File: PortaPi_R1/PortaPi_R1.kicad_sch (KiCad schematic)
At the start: 9 parts, among them J1 Raspberry_Pi_2_3, J2 USB_C_Receptacle, J3 AudioJack2_Ground, SW1 SW_Push, SW2 SW_Slide_DPDT, U1 BQ24072RGT, U2 TPS61252DSG, U3 LTC2942

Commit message: additions
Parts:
- added U4: BME680, Package_LGA:Bosch_LGA-8_3x3mm_P0.8mm_ClockwisePinNumbering, symbol Sensor:BME680
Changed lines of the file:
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@@
+	)
+	(symbol
+		(lib_id "Sensor:BME680")
+		(at 77.47 166.37 0)
+		(unit 1)
+		(exclude_from_sim no)
+		(in_bom yes)
+		(on_board yes)
+		(dnp no)
+		(fields_autoplaced yes)
+		(property "Reference" "U4"
+			(at 66.04 165.0999 0)
+			(effects
+				(font
+					(size 1.27 1.27)
+				)
+				(justify right)
+			)
+		)
+		(property "Value" "BME680"
+			(at 66.04 167.6399 0)
+			(effects
+				(font
+					(size 1.27 1.27)
+				)
+				(justify right)
+			)
+		)
+		(property "Footprint" "Package_LGA:Bosch_LGA-8_3x3mm_P0.8mm_ClockwisePinNumbering"
+			(at 114.3 177.8 0)
+			(effects
+				(font
+					(size 1.27 1.27)
+				)
+				(hide yes)
+			)
+		)
+		(property "Datasheet" "https://ae-bst.resource.bosch.com/media/_tech/media/datasheets/BST-BME680-DS001.pdf"
+			(at 77.47 171.45 0)
+			(effects
+				(font
+					(size 1.27 1.27)
+				)
+				(hide yes)
+			)
+		)
+		(property "Description" "4-in-1 sensor, gas, humidity, pressure, temperature, I2C and SPI interface, 1.71-3.6V, LGA-8"
+			(at 77.47 166.37 0)
+			(effects
+				(font
+					(size 1.27 1.27)
+				)
+				(hide yes)
+			)
+		)
+		(pin "4"
+		)
+		(pin "8"
+		)
+		(pin "5"
+		)
+		(pin "6"
+		)
+		(pin "2"
+		)
+		(pin "7"
+		)
+		(pin "1"
+		)
+		(pin "3"
+		)
+		(instances
+			(project ""
+				(path "/aef56874-4e02-4e4a-b6dd-7772aaa5a84e"
+					(reference "U4")
+					(unit 1)
+				)
+			)
+		)
 	)
 	(symbol

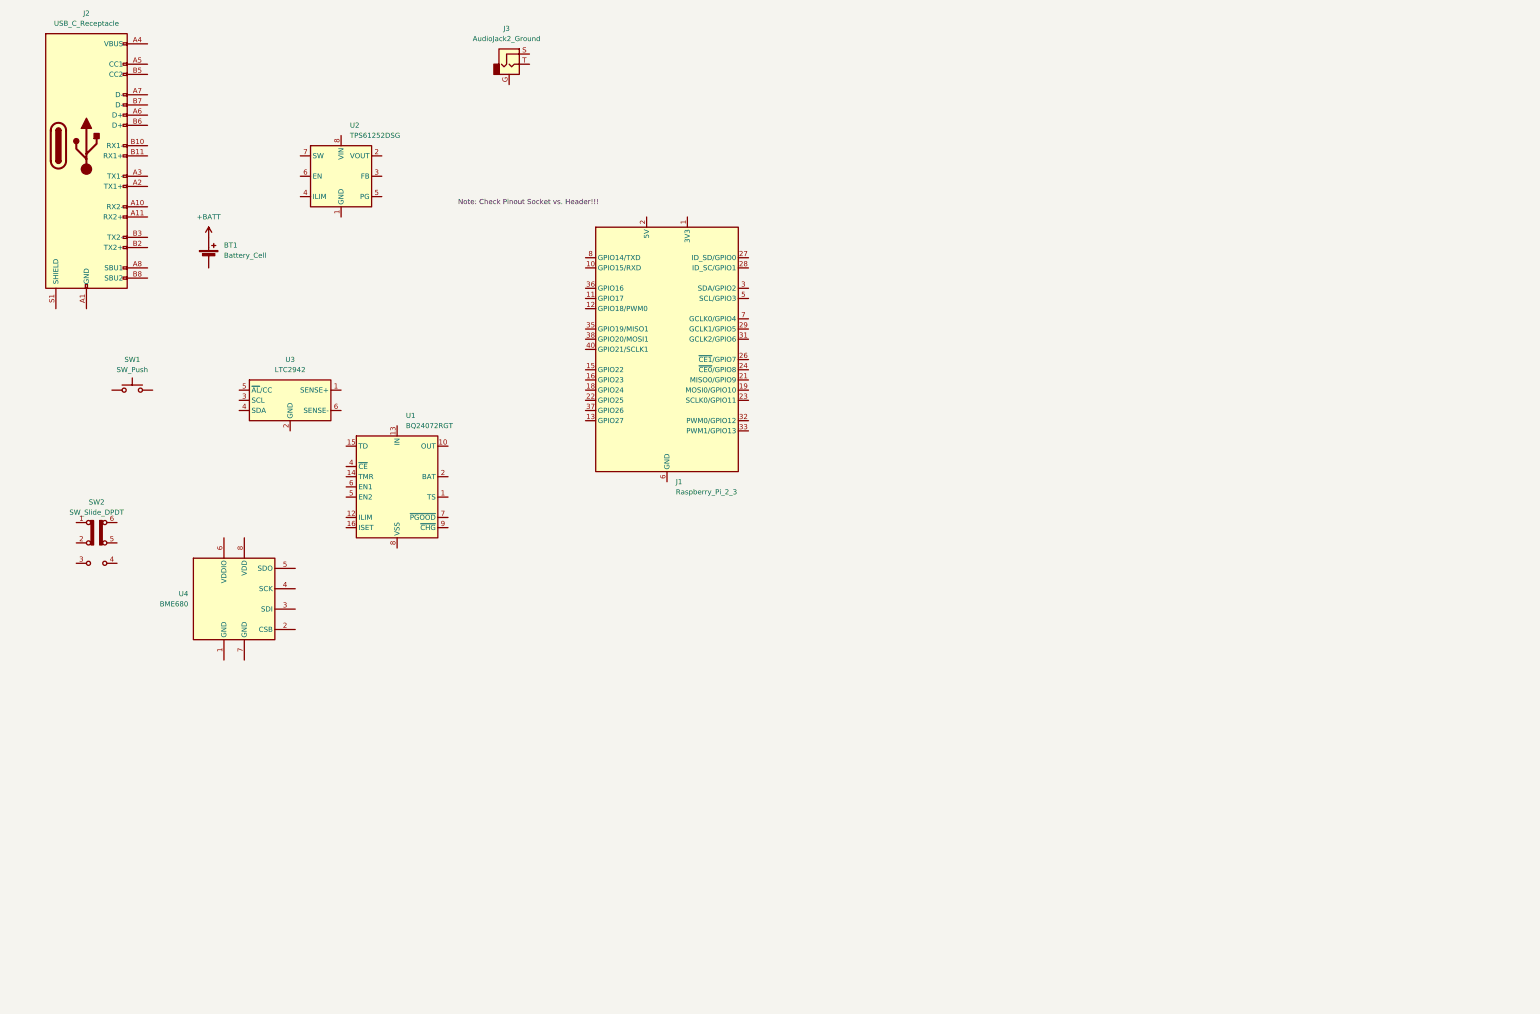
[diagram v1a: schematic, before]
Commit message: designed power path/regulator ect...
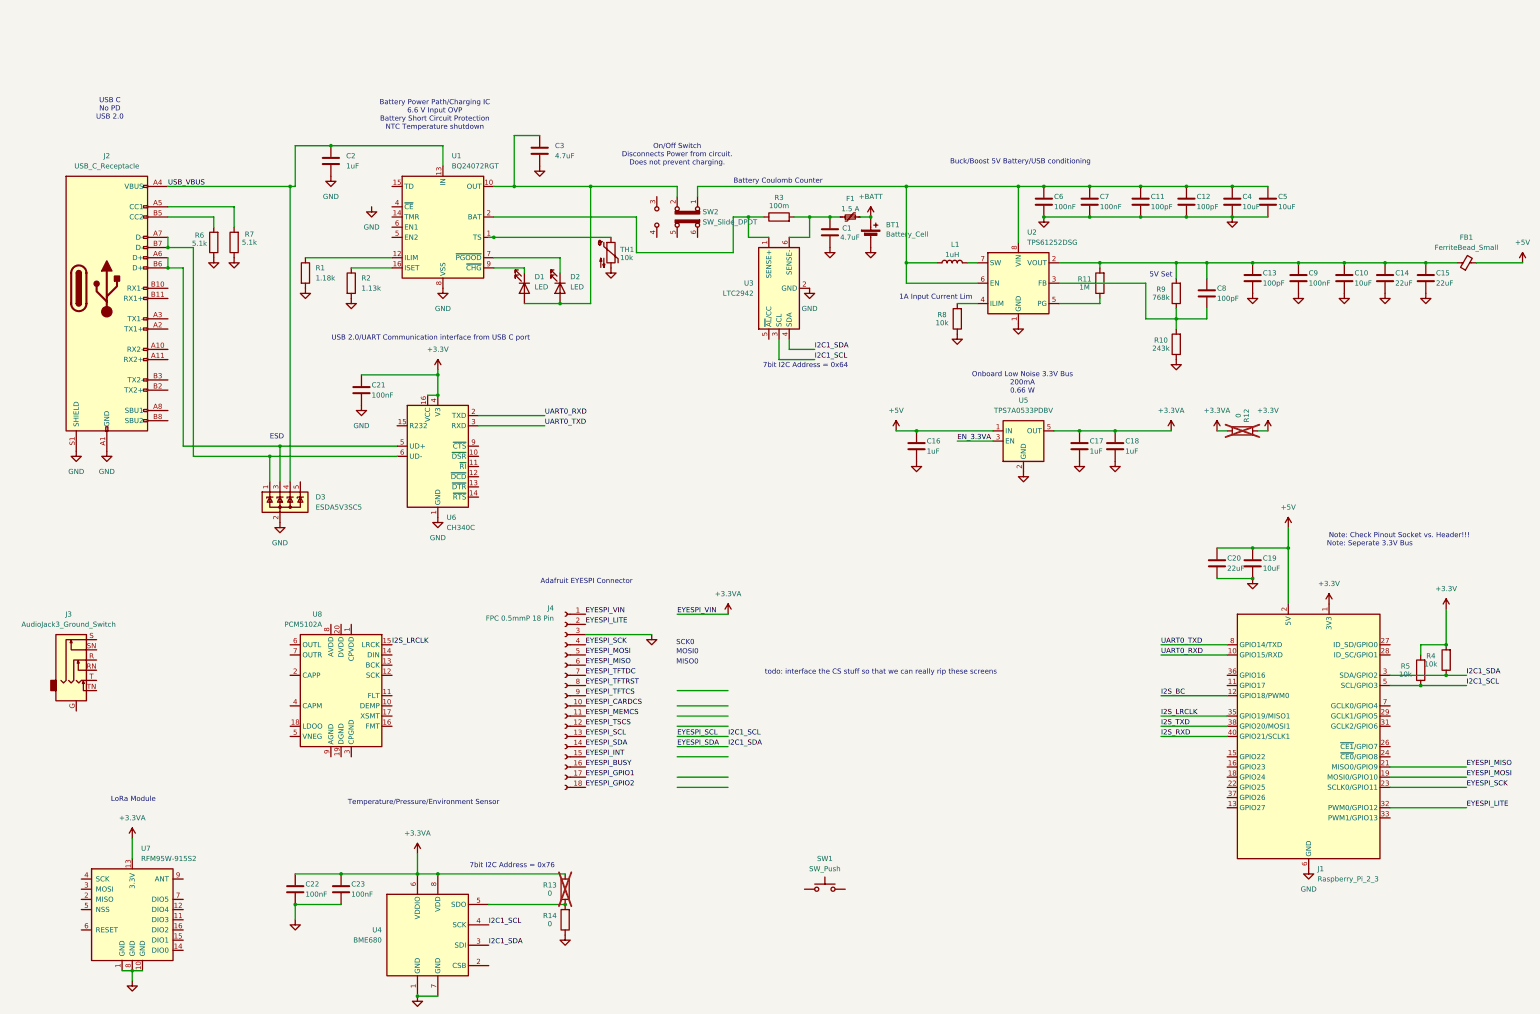
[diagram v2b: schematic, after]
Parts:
- removed J3: AudioJack2_Ground, symbol Connector_Audio:AudioJack2_Ground
- added C1, C3: 4.7uF, symbol Device:C
- added C10, C19, C4, C5: 10uF, symbol Device:C
- added C11, C12, C13, C8: 100pF, symbol Device:C
- added C14, C15, C20: 22uF, symbol Device:C
- added C16, C17, C18, C2: 1uF, symbol Device:C
- added C21, C22, C23, C6, C7, C9: 100nF, symbol Device:C
- added D1, D2: LED, symbol Device:LED
- added D3: ESDA5V3SC5, Package_TO_SOT_SMD:SOT-23-5, symbol Power_Protection:ESDA5V3SC5
- added F1: 1.5 A, symbol Device:Polyfuse_Small
- added FB1: FerriteBead_Small, symbol Device:FerriteBead_Small
- added J3: AudioJack3_Ground_Switch, symbol Connector_Audio:AudioJack3_Ground_Switch
- added J4: FPC 0.5mmP 18 Pin, Connector_FFC-FPC:TE_1-1734839-8_1x18-1MP_P0.5mm_Horizontal, symbol Connector:Conn_01x18_Socket
- added L1: 1uH, symbol Device:L
- added R1: 1.18k, symbol Device:R
- added R10: 243k, symbol Device:R
- added R11: 1M, symbol Device:R
- added R12, R13, R14: 0, symbol Device:R
- added R2: 1.13k, symbol Device:R
- added R3: 100m, symbol Device:R
- added R4, R5, R8: 10k, symbol Device:R
- added R6, R7: 5.1k, symbol Device:R
- added R9: 768k, symbol Device:R
- added TH1: 10k, symbol Device:Thermistor_NTC
- added U5: TPS7A0533PDBV, Package_TO_SOT_SMD:SOT-23-5, symbol Regulator_Linear:TPS7A0533PDBV
- added U6: CH340C, Package_SO:SOIC-16_3.9x9.9mm_P1.27mm, symbol Interface_USB:CH340C
- added U7: RFM95W-915S2, RF_Module:HOPERF_RFM9XW_SMD, symbol RF_Module:RFM95W-915S2
- added U8: PCM5102A, Package_SO:TSSOP-20_4.4x6.5mm_P0.65mm, symbol Audio:PCM5102A
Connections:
- net +BATT: now also F1.2
- net GND: now reaches U4.1 (GND)
- net GND: now also BT1.2 (-), J1.14 (GND), J1.20 (GND), J1.25 (GND), J1.30 (GND), J1.34 (GND), J1.39 (GND), J1.6 (GND), J1.9 (GND), J2.A1 (GND), J2.A12 (GND), J2.B1 (GND), J2.B12 (GND), J2.S1 (SHIELD), U1.17 (VSS), U1.8 (VSS), U2.1 (GND), U2.9 (GND), U3.2 (GND), U4.7 (GND), C1.2, C10.2, C11.2, C12.2, C13.2, C14.2, C15.2, C16.2, C17.2, C18.2, C19.2, C2.2, C20.2, C21.2, C22.2, C23.2, C3.2, C4.2, C5.2, C6.2, C7.2, C9.2, D3.2 (A), J4.3 (Pin_3), R1.2, R10.1, R14.1, R2.2, R6.1, R7.1, R8.1, TH1.2, U5.2 (GND), U6.1 (GND), U7.1 (GND), U7.10 (GND), U7.8 (GND)
- net EYESPI_SDA: now reaches U4.3 (SDI)
- net EYESPI_SDA: now also J1.3 (SDA/GPIO2), U3.4 (SDA), J4.14 (Pin_14), R4.1
- net EYESPI_SCL: now reaches U4.4 (SCK)
- net EYESPI_SCL: now also J1.5 (SCL/GPIO3), U3.3 (SCL), J4.13 (Pin_13), R5.1
- net at U4.5 (SDO): now also R13.1, R14.2
- net +3.3VA: now reaches U4.6 (VDDIO)
- net +3.3VA: now also U4.8 (VDD), C17.1, C18.1, C22.1, C23.1, J4.1 (Pin_1), R12.1, R13.2, U5.5 (OUT), U7.13 (3.3V)
- net at U2.2 (VOUT): now also C10.1, C13.1, C14.1, C15.1, C8.1, C9.1, FB1.1, R11.2, R9.2
- net at U2.3 (FB): now also C8.2, R10.2, R9.1
- net at U2.4 (ILIM): now also R8.2
- net at U2.5 (PG): now also R11.1
- net at U2.6 (EN): now also SW2.1 (A), U2.8 (VIN), C11.1, C12.1, C4.1, C5.1, C6.1, C7.1, L1.1
- net at U2.7 (SW): now also L1.2
- net at SW2.2 (B): now also U1.10 (OUT), U1.11 (OUT), C3.1, D1.2 (A), D2.2 (A)
- net USB_VBUS: now reaches J2.A4 (VBUS), J2.A9 (VBUS), J2.B4 (VBUS), J2.B9 (VBUS)
- net USB_VBUS: now also U1.13 (IN), C2.1, D3.4 (K)
- net at J2.A5 (CC1): now also R7.2
- net at J2.A6 (D+): now also J2.B6 (D+), D3.3 (K), U6.5 (UD+)
- net at J2.A7 (D-): now also J2.B7 (D-), D3.1 (K), U6.6 (UD-)
- net at J2.B5 (CC2): now also R6.2
- net +3.3V: now reaches J1.1 (3V3), J1.17 (3V3)
- net +3.3V: now also C21.1, R12.2, R4.2, R5.2, U6.16 (VCC), U6.4 (V3)
- net UART0_RXD: now reaches J1.10 (GPIO15/RXD)
- net UART0_RXD: now also U6.2 (TXD)
- net I2S_BC: now reaches J1.12 (GPIO18/PWM0)
- net EYESPI_MOSI: now reaches J1.19 (MOSI0/GPIO10)
- net EYESPI_MOSI: now also J4.5 (Pin_5)
- net +5V: now reaches J1.2 (5V), J1.4 (5V)
- net +5V: now also C16.1, C19.1, C20.1, FB1.2, U5.1 (IN)
- net EYESPI_MISO: now reaches J1.21 (MISO0/GPIO9)
- net EYESPI_MISO: now also J4.6 (Pin_6)
- net EYESPI_SCK: now reaches J1.23 (SCLK0/GPIO11)
- net EYESPI_SCK: now also J4.4 (Pin_4)
- net EYESPI_LITE: now reaches J1.32 (PWM0/GPIO12)
- net EYESPI_LITE: now also J4.2 (Pin_2)
- net I2S_LRCLK: now reaches J1.35 (GPIO19/MISO1)
- net I2S_LRCLK: now also U8.15 (LRCK)
- net I2S_TXD: now reaches J1.38 (GPIO20/MOSI1)
- net I2S_RXD: now reaches J1.40 (GPIO21/SCLK1)
- net UART0_TXD: now reaches J1.8 (GPIO14/TXD)
- net UART0_TXD: now also U6.3 (RXD)
- net at U1.1 (TS): now also TH1.1
- net at U1.12 (ILIM): now also R1.1
- net at U1.16 (ISET): now also R2.1
- net at U1.2 (BAT), U1.3 (BAT): now also U3.1 (SENSE+), R3.1
- net at U1.7 (~{PGOOD}): now also D2.1 (K)
- net at U1.9 (~{CHG}): now also D1.1 (K)
- net at U3.6 (SENSE-): now also C1.1, F1.1, R3.2
- new net EN_3.3VA: U5.3 (EN)
- new net EYESPI_BUSY: J4.16 (Pin_16)
- new net EYESPI_CARDCS: J4.10 (Pin_10)
- new net EYESPI_GPIO1: J4.17 (Pin_17)
- new net EYESPI_GPIO2: J4.18 (Pin_18)
- new net EYESPI_INT: J4.15 (Pin_15)
- new net EYESPI_MEMCS: J4.11 (Pin_11)
- new net EYESPI_TFTCS: J4.9 (Pin_9)
- new net EYESPI_TFTDC: J4.7 (Pin_7)
- new net EYESPI_TFTRST: J4.8 (Pin_8)
- new net EYESPI_TSCS: J4.12 (Pin_12)
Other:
- note added: "1A Input Current Lim"
- note added: "5V Set"
- note added: "7bit I2C Address = 0x64"
- note added: "7bit I2C Address = 0x76"
- note added: "Adafruit EYESPI Connector"
- note added: "Battery Coulomb Counter"
- note added: "Battery Power Path/Charging IC 6.6 V Input OVP Battery Short Circuit Protection NTC Temperature shutdown"
- note added: "Buck/Boost 5V Battery/USB conditioning"
- note added: "ESD"
- note added: "LoRa Module"
- note added: "MISO0"
- note added: "MOSI0"
- note added: "Note: Seperate 3.3V Bus"
- note added: "On/Off Switch Disconnects Power from circuit. Does not prevent charging."
- note added: "Onboard Low Noise 3.3V Bus 200mA 0.66 W"
- note added: "SCK0"
- note added: "Temperature/Pressure/Environment Sensor"
- note added: "USB 2.0/UART Communication interface from USB C port"
- note added: "USB C No PD USB 2.0"
- note added: "todo: interface the CS stuff so that we can really rip these screens"
- moved on the sheet: BT1, J1, J2, SW1, SW2, U1, U2, U3, U4

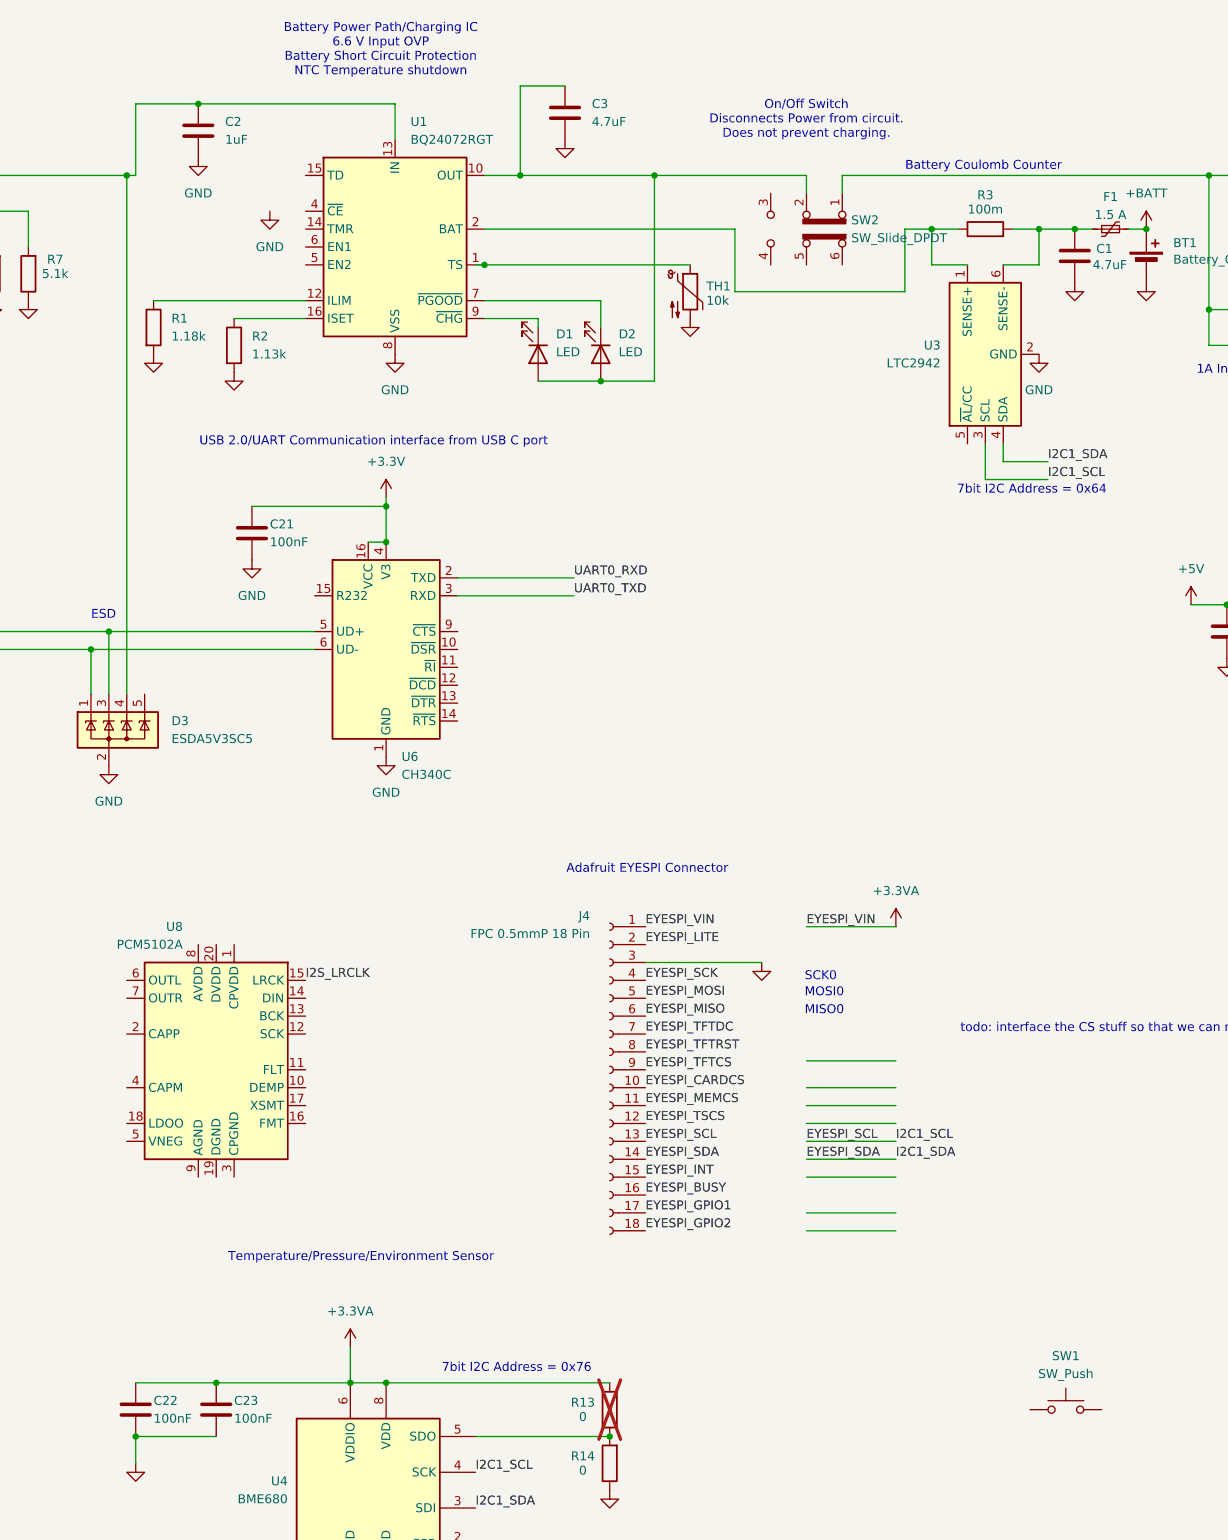
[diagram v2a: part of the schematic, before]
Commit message: created altoids tin and boundary as footprints
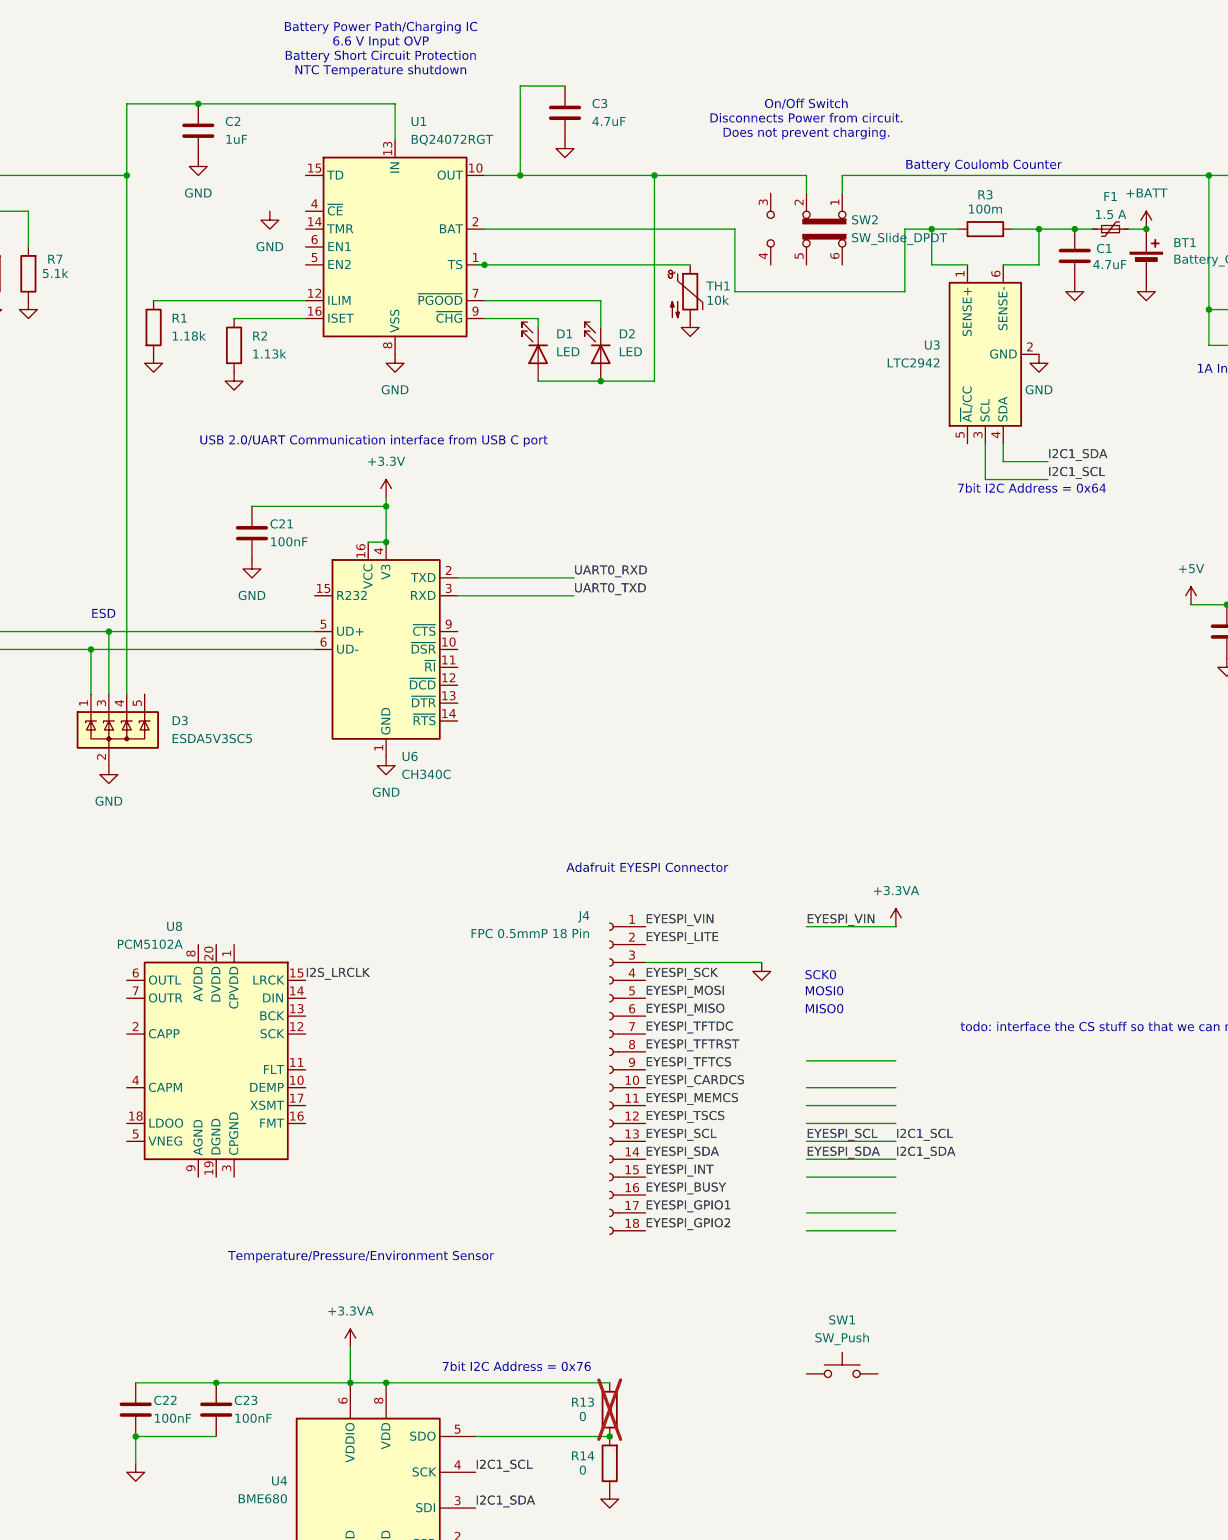
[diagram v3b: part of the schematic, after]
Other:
- moved on the sheet: SW1
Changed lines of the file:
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@@
-	(wire
-		(pts
-			(xy 91.44 63.5) (xy 92.71 63.5)
-		)
-		(stroke
-			(width 0)
-			(type default)
-		)
-	)
 	(wire
 		(pts
@@
 	(wire
 		(pts
-			(xy 101.6 53.34) (xy 92.71 53.34)
+			(xy 101.6 53.34) (xy 91.44 53.34)
 		)
 		(stroke
@@
 	(wire
 		(pts
-			(xy 92.71 53.34) (xy 92.71 63.5)
+			(xy 91.44 53.34) (xy 91.44 63.5)
 		)
 		(stroke
@@
 	(symbol
 		(lib_id "Switch:SW_Push")
-		(at 224.79 238.76 0)
+		(at 193.04 233.68 0)
 		(unit 1)
 		(exclude_from_sim no)
@@
 		(fields_autoplaced yes)
 		(property "Reference" "SW1"
-			(at 224.79 231.14 0)
+			(at 193.04 226.06 0)
 			(effects
 				(font
@@
 		)
 		(property "Value" "SW_Push"
-			(at 224.79 233.68 0)
+			(at 193.04 228.6 0)
 			(effects
 				(font
@@
 		)
 		(property "Footprint" ""
-			(at 224.79 233.68 0)
+			(at 193.04 228.6 0)
 			(effects
 				(font
@@
 		)
 		(property "Datasheet" "~"
-			(at 224.79 233.68 0)
+			(at 193.04 228.6 0)
 			(effects
 				(font
@@
 		)
 		(property "Description" "Push button switch, generic, two pins"
-			(at 224.79 238.76 0)
+			(at 193.04 233.68 0)
 			(effects
 				(font
